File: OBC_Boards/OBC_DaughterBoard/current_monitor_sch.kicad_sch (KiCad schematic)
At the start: 5 parts, among them U3 MCP3008

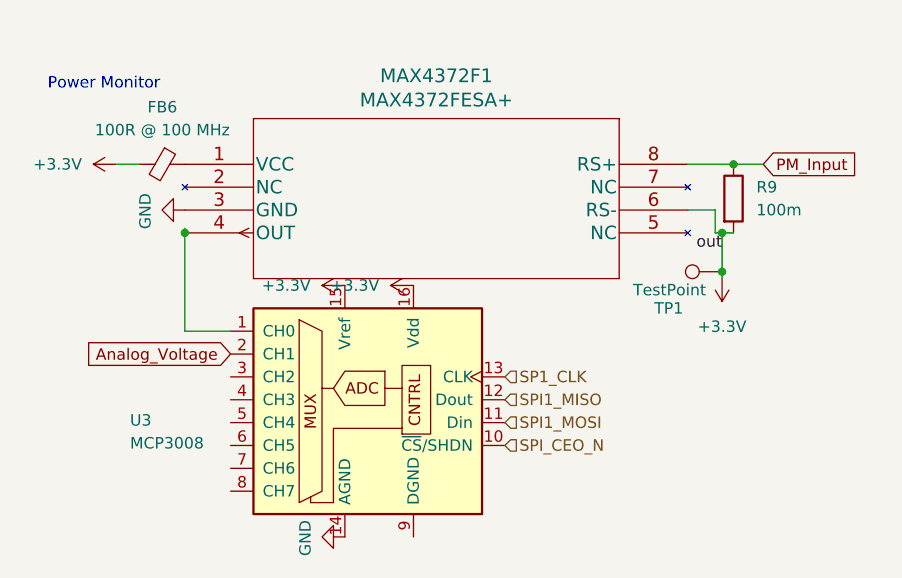
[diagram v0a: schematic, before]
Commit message: obc: daughterboard: clean up all schematics for easier reworks
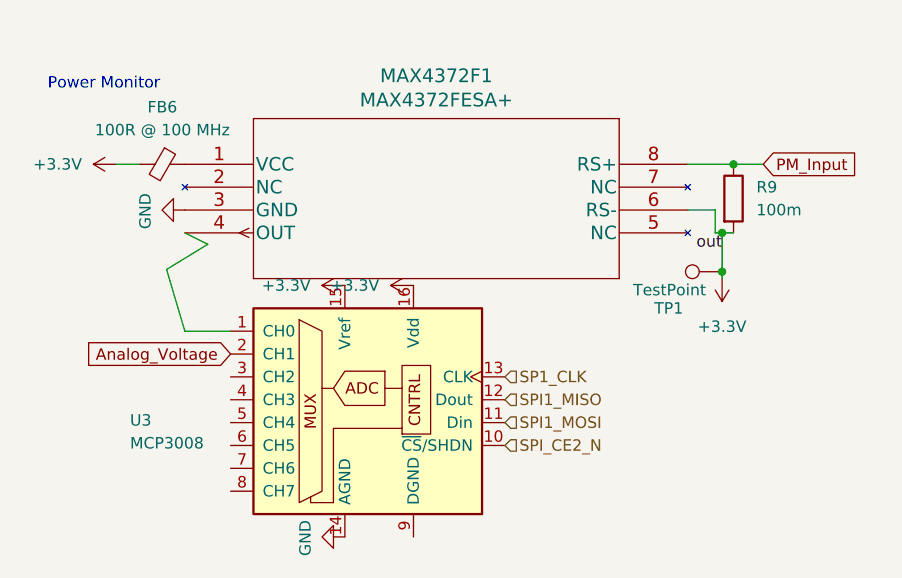
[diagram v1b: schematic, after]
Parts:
- MAX4372F1: footprint Max4372:Maxim-MAX4372FESA+-Level_A -> Daughterboard_footprints:Maxim-MAX4372FESA+-Level_A
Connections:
- net SPI_CEO_N renamed SPI_CE2_N
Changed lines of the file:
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@@
 (kicad_sch (version 20211123) (generator eeschema)
   (paper "A4")
-  (junction (at 125.222 87.376) (diameter 0) (color 0 0 0 0)
-  )
   (junction (at 184.912 91.694) (diameter 0) (color 0 0 0 0)
   )
@@
     (stroke (width 0) (type default) (color 0 0 0 0))
   )
-  (wire (pts (xy 181.102 84.836) (xy 184.15 84.836))
+  (wire (pts (xy 127.762 88.646) (xy 125.222 87.376))
     (stroke (width 0) (type default) (color 0 0 0 0))
   )
-  (wire (pts (xy 125.222 86.868) (xy 125.222 87.376))
+  (wire (pts (xy 181.102 84.836) (xy 184.15 84.836))
     (stroke (width 0) (type default) (color 0 0 0 0))
   )
@@
     (stroke (width 0) (type default) (color 0 0 0 0))
   )
-  (wire (pts (xy 125.222 87.376) (xy 125.222 98.298))
+  (wire (pts (xy 123.19 91.44) (xy 125.222 98.298))
     (stroke (width 0) (type default) (color 0 0 0 0))
   )
@@
   )
   (wire (pts (xy 189.484 79.756) (xy 186.182 79.756))
+    (stroke (width 0) (type default) (color 0 0 0 0))
+  )
+  (wire (pts (xy 123.19 91.44) (xy 127.762 88.646))
     (stroke (width 0) (type default) (color 0 0 0 0))
   )
@@
     (effects (font (size 1.27 1.27)) (justify left))
   )
-  (hierarchical_label "SPI_CEO_N" (shape input) (at 160.782 110.998 0)
+  (hierarchical_label "SPI_CE2_N" (shape input) (at 160.782 110.998 0)
     (effects (font (size 1.27 1.27)) (justify left))
   )
@@
       (effects (font (size 1.524 1.524)))
     )
-    (property "Footprint" "Max4372:Maxim-MAX4372FESA+-Level_A" (id 2) (at 136.652 65.786 0)
+    (property "Footprint" "Daughterboard_footprints:Maxim-MAX4372FESA+-Level_A" (id 2) (at 136.652 65.786 0)
       (effects (font (size 1.524 1.524)) hide)
     )

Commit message: footprint fix
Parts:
- U3: footprint MCP3008:Microchip-MCP3008-I_P-Manufacturer_Recommended -> Daughterboard_footprints:Microchip-MCP3008-I_P-Manufacturer_Recommended
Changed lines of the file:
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@@
       (effects (font (size 1.27 1.27)) (justify left))
     )
-    (property "Footprint" "MCP3008:Microchip-MCP3008-I_P-Manufacturer_Recommended" (id 2) (at 148.082 103.378 0)
+    (property "Footprint" "Daughterboard_footprints:Microchip-MCP3008-I_P-Manufacturer_Recommended" (id 2) (at 148.082 103.378 0)
       (effects (font (size 1.27 1.27)) hide)
     )

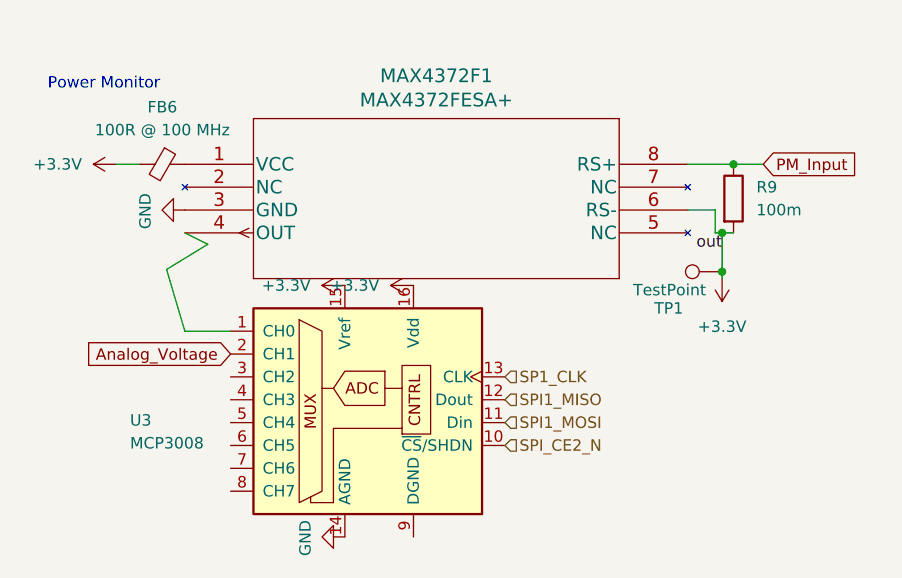
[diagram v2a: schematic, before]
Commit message: adding charging circuit
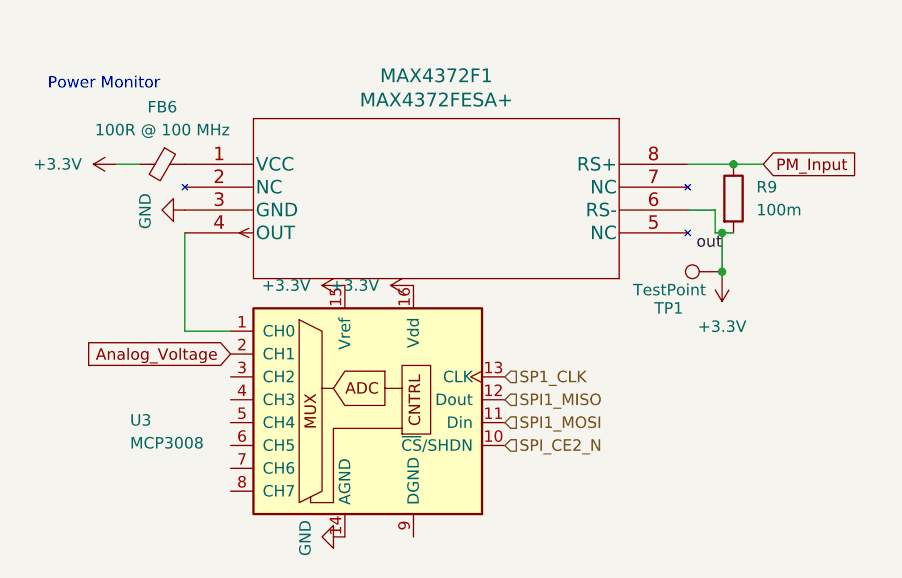
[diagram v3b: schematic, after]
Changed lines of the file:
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@@
-    (stroke (width 0) (type default) (color 0 0 0 0))
-  )
-  (wire (pts (xy 127.762 88.646) (xy 125.222 87.376))
     (stroke (width 0) (type default) (color 0 0 0 0))
   )
@@
     (stroke (width 0) (type default) (color 0 0 0 0))
   )
-  (wire (pts (xy 125.222 98.298) (xy 130.302 98.298))
-    (stroke (width 0) (type default) (color 0 0 0 0))
-  )
   (wire (pts (xy 184.912 91.694) (xy 184.912 92.456))
     (stroke (width 0) (type default) (color 0 0 0 0))
   )
-  (wire (pts (xy 123.19 91.44) (xy 125.222 98.298))
+  (wire (pts (xy 125.222 87.376) (xy 125.222 98.298))
     (stroke (width 0) (type default) (color 0 0 0 0))
   )
@@
     (stroke (width 0) (type default) (color 0 0 0 0))
   )
-  (wire (pts (xy 123.19 91.44) (xy 127.762 88.646))
+  (wire (pts (xy 125.222 98.298) (xy 130.302 98.298))
     (stroke (width 0) (type default) (color 0 0 0 0))
   )

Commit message: Replaced mcp3008 footprint to smd chip
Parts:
- U3: footprint Daughterboard_footprints:Microchip-MCP3008-I_P-Manufacturer_Recommended -> Daughterboard_footprints:Microchip-MCP3008-I_SL-Level_A
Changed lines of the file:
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@@
       (effects (font (size 1.27 1.27)) (justify left))
     )
-    (property "Footprint" "Daughterboard_footprints:Microchip-MCP3008-I_P-Manufacturer_Recommended" (id 2) (at 148.082 103.378 0)
+    (property "Footprint" "Daughterboard_footprints:Microchip-MCP3008-I_SL-Level_A" (id 2) (at 148.082 103.378 0)
       (effects (font (size 1.27 1.27)) hide)
     )

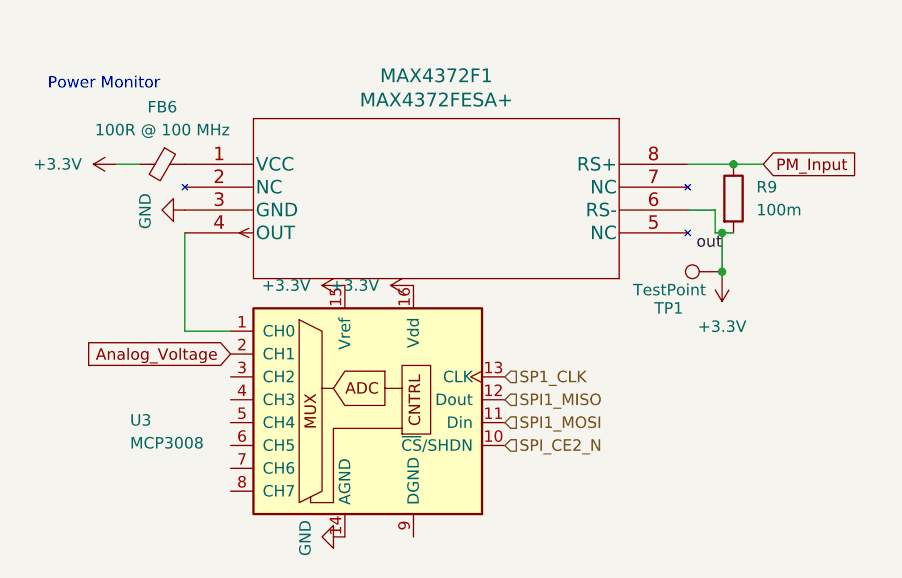
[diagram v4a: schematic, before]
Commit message: Adding data traces
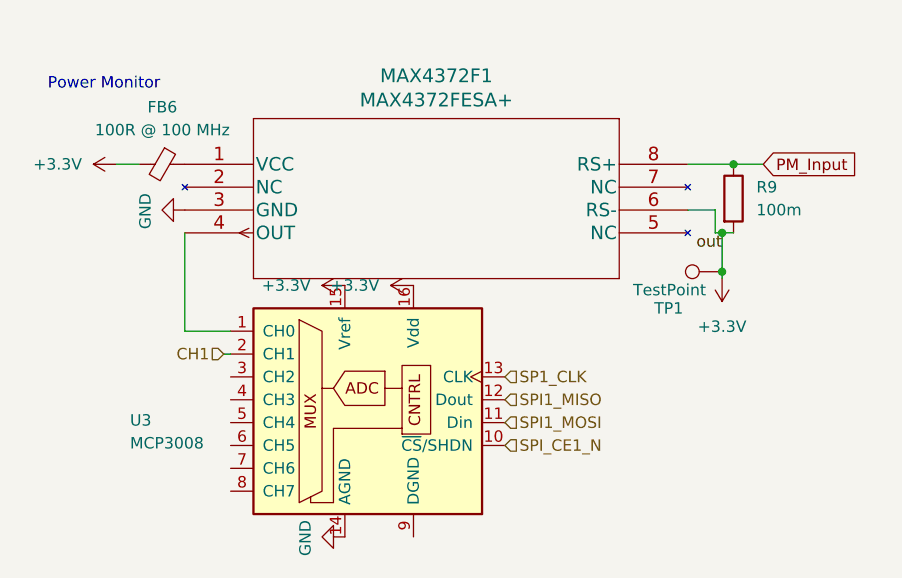
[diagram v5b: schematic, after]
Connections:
- net Analog_Voltage renamed CH1
- net SPI_CE2_N renamed SPI_CE1_N
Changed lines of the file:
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@@
+    (stroke (width 0) (type default) (color 0 0 0 0))
+  )
+  (wire (pts (xy 129.54 100.838) (xy 130.302 100.838))
     (stroke (width 0) (type default) (color 0 0 0 0))
   )
@@
   (label "out" (at 184.912 89.408 180)
     (effects (font (size 1.27 1.27)) (justify right bottom))
-  )
-  (global_label "Analog_Voltage" (shape input) (at 130.302 100.838 180) (fields_autoplaced)
-    (effects (font (size 1.27 1.27)) (justify right))
-    (property "Intersheet References" "${INTERSHEET_REFS}" (id 0) (at 113.556 100.9174 0)
-      (effects (font (size 1.27 1.27)) (justify right) hide)
-    )
   )
   (global_label "PM_Input" (shape input) (at 189.484 79.756 0) (fields_autoplaced)
@@
     (effects (font (size 1.27 1.27)) (justify left))
   )
-  (hierarchical_label "SPI_CE2_N" (shape input) (at 160.782 110.998 0)
+  (hierarchical_label "SPI_CE1_N" (shape input) (at 160.782 110.998 0)
     (effects (font (size 1.27 1.27)) (justify left))
   )
+  (hierarchical_label "CH1" (shape input) (at 129.54 100.838 180)
+    (effects (font (size 1.27 1.27)) (justify right))
+  )
   (hierarchical_label "SP1_CLK" (shape input) (at 160.782 103.378 0)

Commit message: Layout completed
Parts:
- TP1: footprint TestPoint:TestPoint_2Pads_Pitch2.54mm_Drill0.8mm -> TestPoint:TestPoint_Pad_2.0x2.0mm
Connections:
- net +3V3: no longer TP1.1
- net PM_Input: now also TP1.1
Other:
- moved on the sheet: TP1
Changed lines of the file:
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@@
 (kicad_sch (version 20211123) (generator eeschema)
   (paper "A4")
-  (junction (at 184.912 91.694) (diameter 0) (color 0 0 0 0)
+  (junction (at 183.388 79.756) (diameter 0) (color 0 0 0 0)
   )
   (junction (at 186.182 79.756) (diameter 0) (color 0 0 0 0)
@@
   (junction (at 184.912 87.376) (diameter 0) (color 0 0 0 0)
   )
-  (wire (pts (xy 181.102 79.756) (xy 186.182 79.756))
+  (wire (pts (xy 181.102 79.756) (xy 183.388 79.756))
     (stroke (width 0) (type default) (color 0 0 0 0))
   )
@@
     (stroke (width 0) (type default) (color 0 0 0 0))
   )
+  (wire (pts (xy 183.388 79.756) (xy 186.182 79.756))
+    (stroke (width 0) (type default) (color 0 0 0 0))
+  )
   (wire (pts (xy 184.15 84.836) (xy 184.15 87.376))
     (stroke (width 0) (type default) (color 0 0 0 0))
   )
-  (wire (pts (xy 184.912 91.694) (xy 184.912 92.456))
-    (stroke (width 0) (type default) (color 0 0 0 0))
-  )
   (wire (pts (xy 125.222 87.376) (xy 125.222 98.298))
     (stroke (width 0) (type default) (color 0 0 0 0))
@@
     (stroke (width 0) (type default) (color 0 0 0 0))
   )
-  (wire (pts (xy 184.912 87.376) (xy 184.912 91.694))
+  (wire (pts (xy 183.388 76.454) (xy 183.388 79.756))
+    (stroke (width 0) (type default) (color 0 0 0 0))
+  )
+  (wire (pts (xy 184.912 87.376) (xy 184.912 92.456))
     (stroke (width 0) (type default) (color 0 0 0 0))
   )
@@
     (effects (font (size 1.27 1.27)) (justify right bottom))
   )
-  (global_label "PM_Input" (shape input) (at 189.484 79.756 0) (fields_autoplaced)
-    (effects (font (size 1.27 1.27)) (justify left))
-    (property "Intersheet References" "${INTERSHEET_REFS}" (id 0) (at 200.3638 79.6766 0)
-      (effects (font (size 1.27 1.27)) (justify left) hide)
-    )
-  )
   (hierarchical_label "SPI1_MISO" (shape input) (at 160.782 105.918 0)
     (effects (font (size 1.27 1.27)) (justify left))
@@
   )
   (hierarchical_label "SP1_CLK" (shape input) (at 160.782 103.378 0)
+    (effects (font (size 1.27 1.27)) (justify left))
+  )
+  (hierarchical_label "PM_Input" (shape bidirectional) (at 189.484 79.756 0)
     (effects (font (size 1.27 1.27)) (justify left))
   )
@@
     (pin "1")
   )
-  (symbol (lib_id "Connector:TestPoint") (at 184.912 91.694 90) (unit 1)
-    (in_bom yes) (on_board yes)
-    (property "Reference" "TP1" (id 0) (at 180.594 95.758 90)
-      (effects (font (size 1.27 1.27)) (justify left))
-    )
-    (property "Value" "TestPoint" (id 1) (at 183.134 93.726 90)
-      (effects (font (size 1.27 1.27)) (justify left))
-    )
-    (property "Footprint" "TestPoint:TestPoint_2Pads_Pitch2.54mm_Drill0.8mm" (id 2) (at 184.912 86.614 0)
-      (effects (font (size 1.27 1.27)) hide)
-    )
-    (property "Datasheet" "~" (id 3) (at 184.912 86.614 0)
-      (effects (font (size 1.27 1.27)) hide)
-    )
+  (symbol (lib_id "Connector:TestPoint") (at 183.388 76.454 0) (unit 1)
+    (in_bom yes) (on_board yes)
+    (property "Reference" "TP1" (id 0) (at 179.324 72.136 90)
+      (effects (font (size 1.27 1.27)) (justify left))
+    )
+    (property "Value" "TestPoint" (id 1) (at 181.356 74.676 90)
+      (effects (font (size 1.27 1.27)) (justify left))
+    )
+    (property "Footprint" "TestPoint:TestPoint_Pad_2.0x2.0mm" (id 2) (at 188.468 76.454 0)
+      (effects (font (size 1.27 1.27)) hide)
+    )
+    (property "Datasheet" "~" (id 3) (at 188.468 76.454 0)
+      (effects (font (size 1.27 1.27)) hide)
+    )
